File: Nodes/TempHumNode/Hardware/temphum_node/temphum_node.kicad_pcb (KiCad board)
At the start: 2 copper layers, 91.6 x 51.3 mm, 69 parts, among them IC1 CC1310F128RGZR, IC2 TPD6E004RSER, J1 TC2050-IDC, U1 MCP73123-22SI/MF, U2 SHT35-DIS-B, U3 TPS22860DBVR, U4 TPS63900DSKR, U5 MCP3421A0T-E/CH, U6 TPS22860DBVR, U7 ECS-240-9-33B-CWN-TR, X1 FC-135R

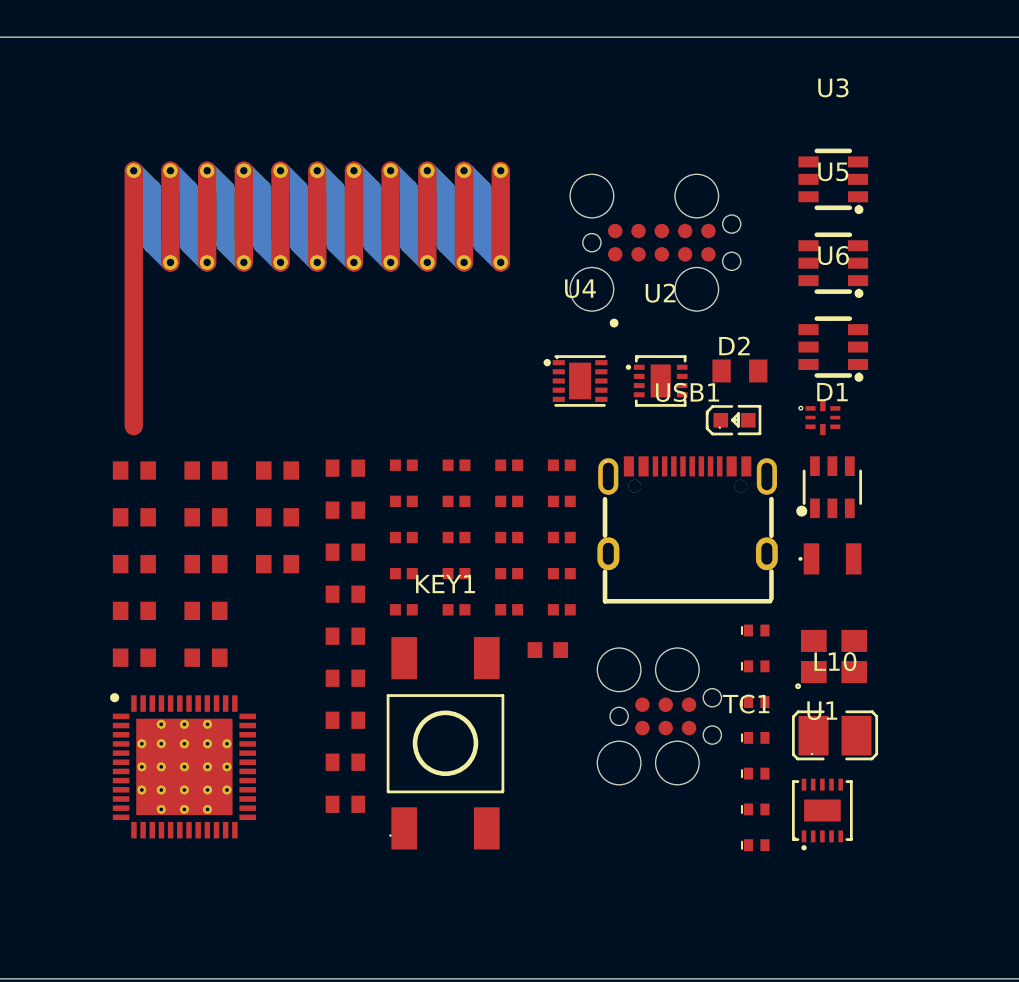
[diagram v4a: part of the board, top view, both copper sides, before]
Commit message: hw(temphum-node): add battery connector (JST B2B-PH-K-S placeholder)
Add JST PH 2.0mm 2-pin top-entry THT connector (LCSC C131337) as the
battery input placeholder. Top-entry chosen (lead internal to the
enclosure). To be confirmed against the actual pack Tue: connector
family (PH vs XH) + which pin is BAT+.

Co-Authored-By: Claude Opus 4.8 (1M context) <noreply@anthropic.com>
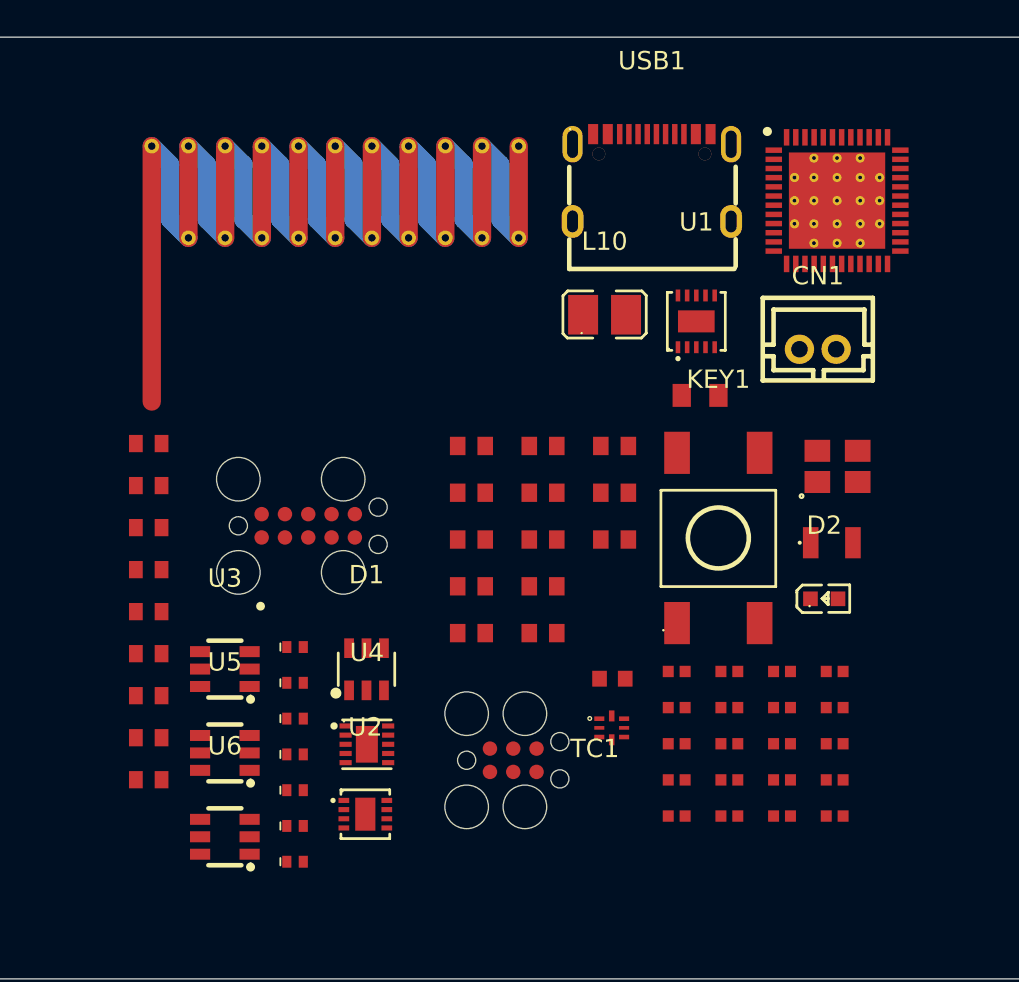
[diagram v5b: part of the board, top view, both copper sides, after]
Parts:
- added CN1: B2B-PH-K-S, SmartHome:CONN-TH_B2B-PH-K-S, F.Cu at (172.6, 33.6)
- moved IC1 47.1 mm to (173.7, 25.5)
- moved U3 42.6 mm to (140.3, 51.0)
- moved U5 42.6 mm to (140.3, 55.6)
- moved U6 42.6 mm to (140.3, 60.1)
- moved U2 28.6 mm to (148.0, 58.9)
- moved U1 27.5 mm to (166.0, 32.0)
- moved D1 27.3 mm to (148.0, 51.0)
- moved L10 26.2 mm to (161.0, 31.7)
- moved L1 25.2 mm to (144.1, 49.8)
- moved L2 25.2 mm to (144.1, 51.7)
- moved L3 25.2 mm to (144.1, 53.7)
- moved L4 25.2 mm to (144.1, 55.6)
- moved L5 25.2 mm to (144.1, 57.6)
- moved L6 25.2 mm to (144.1, 59.5)
- moved L7 25.2 mm to (144.1, 61.5)
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
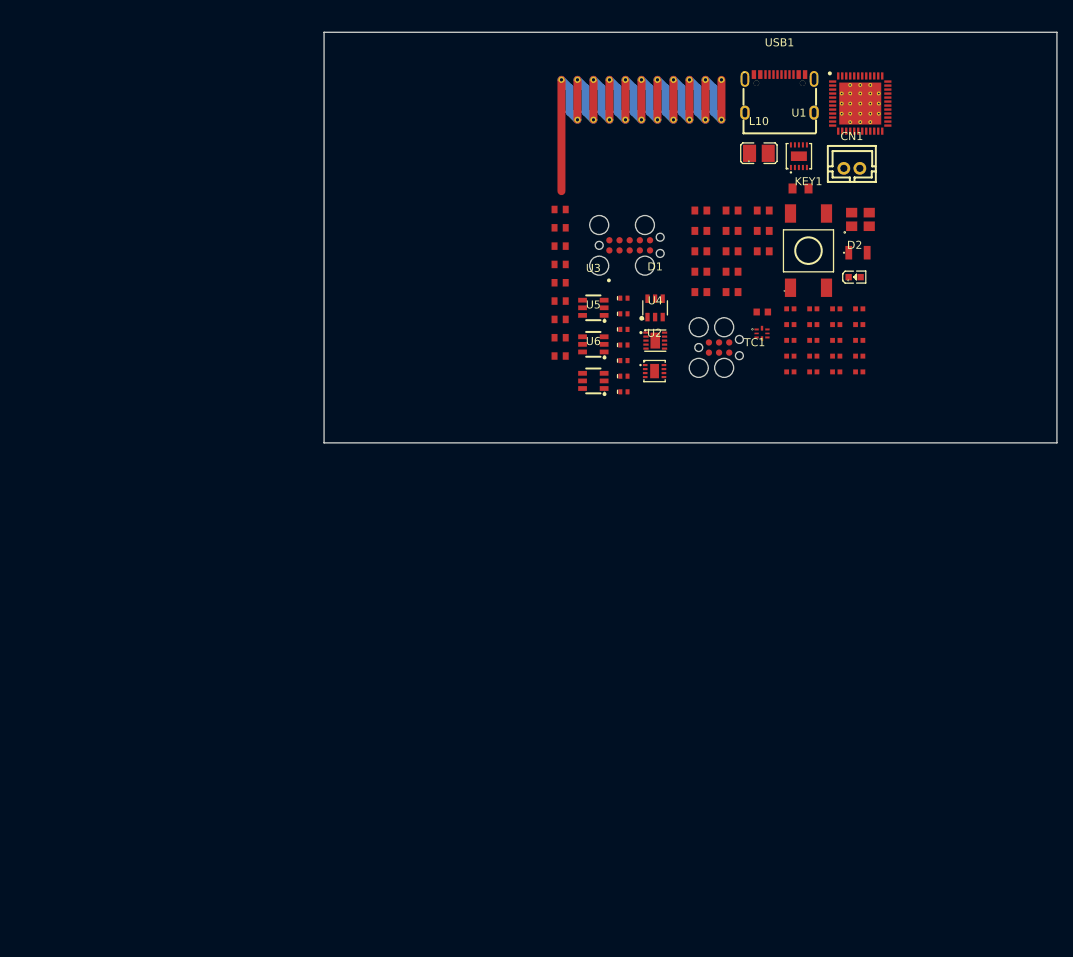
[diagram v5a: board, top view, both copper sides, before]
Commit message: hw(temphum): rev2 node schematic + PCB layout + KiCad lib parts
Full rev-2 T&H node hardware: wired schematic, 4-layer PCB layout
(RF-first placement, GND stitching, DRC-clean). Library additions:
JST XH 2.5mm connector (C158012), R_0402, and imported/perfected
footprints. USB-C center holes fixed to NPTH (annular-ring clean).

Co-Authored-By: Claude Opus 4.8 (1M context) <noreply@anthropic.com>
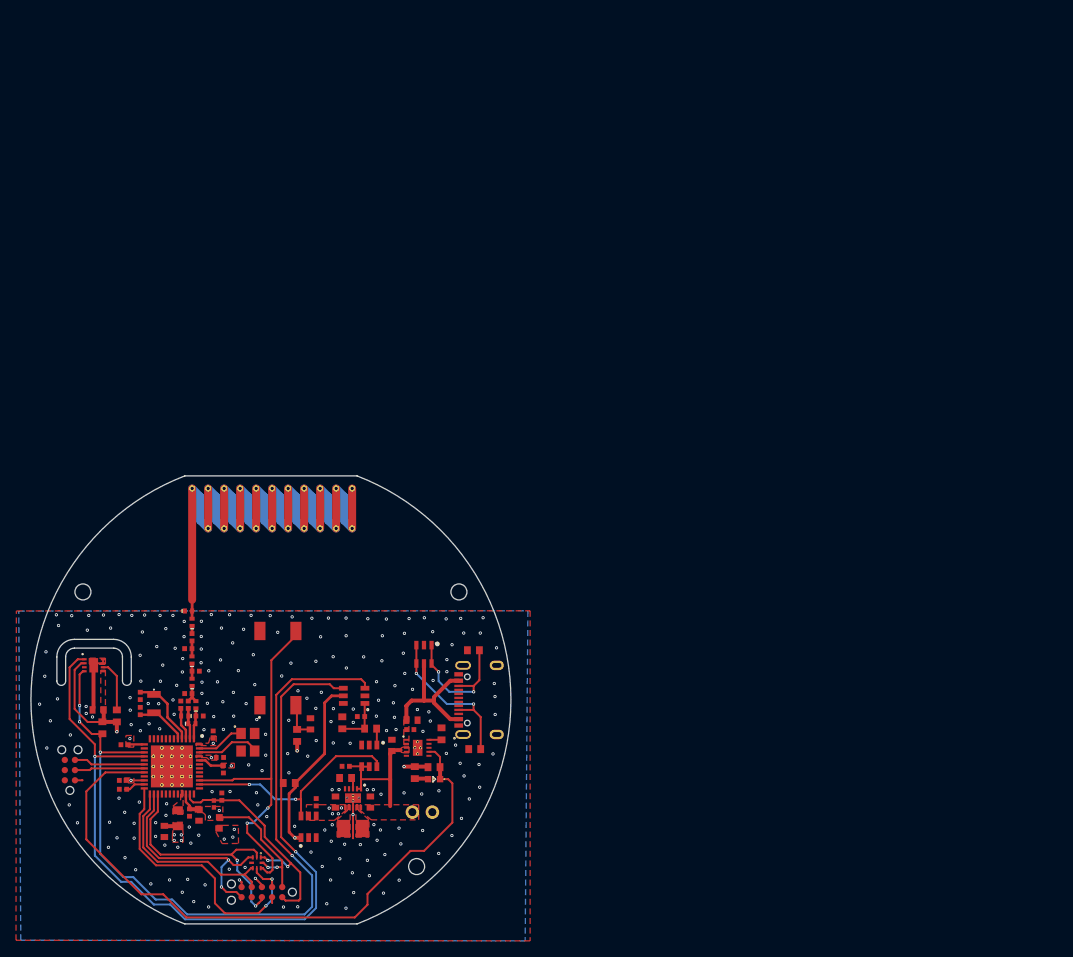
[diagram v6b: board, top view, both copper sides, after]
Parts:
- removed CN1: B2B-PH-K-S, SmartHome:CONN-TH_B2B-PH-K-S
- added CN2: B2B-XH-A, SmartHome:CONN-TH_B2B-XH-A-LF-SN, B.Cu at (118.9, 114.0)
- C25: footprint SmartHome:C_0603 -> SmartHome:C_0402
- R13: footprint SmartHome:R_0603 -> SmartHome:R_0402
- moved IC1 119.5 mm to (87.6, 108.3), turned to -90 degrees
- moved L11 110.7 mm to (88.4, 114.8), turned to -90 degrees
- moved C15 105.3 mm to (81.5, 111.2), turned to 180 degrees
- moved X1 104.5 mm to (85.4, 100.5), turned to -90 degrees
- moved C16 101.4 mm to (81.7, 105.6), turned to 180 degrees
- moved U7 100.7 mm to (97.1, 105.3), turned to -90 degrees
- moved C5 99.9 mm to (81.5, 110.1), turned to 180 degrees
- moved C14 99.5 mm to (83.7, 101.4), turned to 90 degrees
- moved L10 98.5 mm to (110.3, 116.1), turned to 180 degrees
- moved C20 97.6 mm to (93.6, 107.2)
- moved R13 97.4 mm to (92.9, 113.0), turned to 90 degrees
- moved TC1 96.8 mm to (74.9, 108.8), turned to 90 degrees
- moved C4 96.8 mm to (89.8, 114.1), turned to -90 degrees
- moved C9 96.1 mm to (83.7, 99.5), turned to -90 degrees
- moved C13 95.7 mm to (88.7, 100.6), turned to 90 degrees
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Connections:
- D1 pad 1: CC1 -> CC2
- D1 pad 3: CC2 -> CC1
- D1 pad 4: CC2 -> CC1
- D1 pad 6: CC1 -> CC2
- IC1 pad 10: PERIPH_EN -> unconnected-(IC1-DIO_5-Pad10)
- IC1 pad 11: nBUTTON -> unconnected-(IC1-DIO_6-Pad11)
- IC1 pad 12: nCHRGSTAT -> unconnected-(IC1-DIO_7-Pad12)
- IC1 pad 15: unconnected-(IC1-DIO_9-Pad15) -> SCL
- IC1 pad 16: unconnected-(IC1-DIO_10-Pad16) -> SDA
- IC1 pad 18: unconnected-(IC1-DIO_12-Pad18) -> UART_TX
- IC1 pad 19: unconnected-(IC1-DIO_13-Pad19) -> UART_RX
- IC1 pad 20: unconnected-(IC1-DIO_14-Pad20) -> nCHRGSTAT
- IC1 pad 21: JTAG_TDO -> unconnected-(IC1-DIO_15-Pad21)
- IC1 pad 26: JTAG_TDI -> JTAG_TDO
- IC1 pad 27: unconnected-(IC1-DIO_17-Pad27) -> JTAG_TDI
- IC1 pad 38: unconnected-(IC1-DIO_25-Pad38) -> PERIPH_EN
- IC1 pad 39: unconnected-(IC1-DIO_26-Pad39) -> nBUTTON
- IC1 pad 6: SCL -> unconnected-(IC1-DIO_1-Pad6)
- IC1 pad 7: SDA -> unconnected-(IC1-DIO_2-Pad7)
- IC1 pad 8: UART_TX -> unconnected-(IC1-DIO_3-Pad8)
- IC1 pad 9: UART_RX -> unconnected-(IC1-DIO_4-Pad9)
- TC1 pad 2: UART_TX -> unconnected-(TC1-~-Pad2)
- TC1 pad 5: unconnected-(TC1-~-Pad5) -> UART_TX
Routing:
- net SCL: track 0.00 -> 102.1 mm, vias 0 -> 4
- net SDA: track 0.00 -> 101.6 mm, vias 0 -> 2
- net nCHRGSTAT: track 0.00 -> 80.8 mm
- net 3V3_SW: track 0.00 -> 76.9 mm, vias 0 -> 2
- net VDDS: track 0.00 -> 63.7 mm, vias 0 -> 7
- net nBUTTON: track 0.00 -> 45.0 mm, vias 0 -> 2
- net JTAG_TMS: track 0.00 -> 36.6 mm, vias 0 -> 2
- net 3V3: track 0.00 -> 36.0 mm, vias 0 -> 9
- net JTAG_TDI: track 0.00 -> 30.6 mm, vias 0 -> 2
- net nRESET: track 0.00 -> 29.6 mm, vias 0 -> 2
- net PERIPH_EN: track 0.00 -> 28.8 mm, vias 0 -> 2
- net JTAG_TDO: track 0.00 -> 28.3 mm, vias 0 -> 2
- net JTAG_TCK: track 0.00 -> 24.4 mm
- net CC1: track 0.00 -> 20.2 mm, vias 0 -> 2
- net VBUS: track 0.00 -> 18.7 mm
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- added copper zone on F.Cu, net 3V3
- added copper zone on In2.Cu, net 3V3
- added copper zone on F.Cu, net 3V3_SW
- added copper zone on F.Cu, net BAT+
- added copper zone on F.Cu, net DCDC_SW
- added copper zone on B.Cu, net GND
- added copper zone on F.Cu, net GND
- added copper zone on In1.Cu, net GND
- added copper zone on In2.Cu, net GND
- added copper zone on F.Cu, net Net-(U4-LX1)
- added copper zone on F.Cu, net Net-(U4-LX2)
- added copper zone on F.Cu, net VBUS
- added copper zone on F.Cu, net VDDR
- added copper zone on In2.Cu, net VDDR
- added copper zone on F.Cu, net VDDS
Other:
- board size 91.6 x 51.3 mm -> 60 x 56 mm
- copper layers 2 -> 4
- board text added: "+"
- board text added: "-"
- board text added: "LiFePO4"

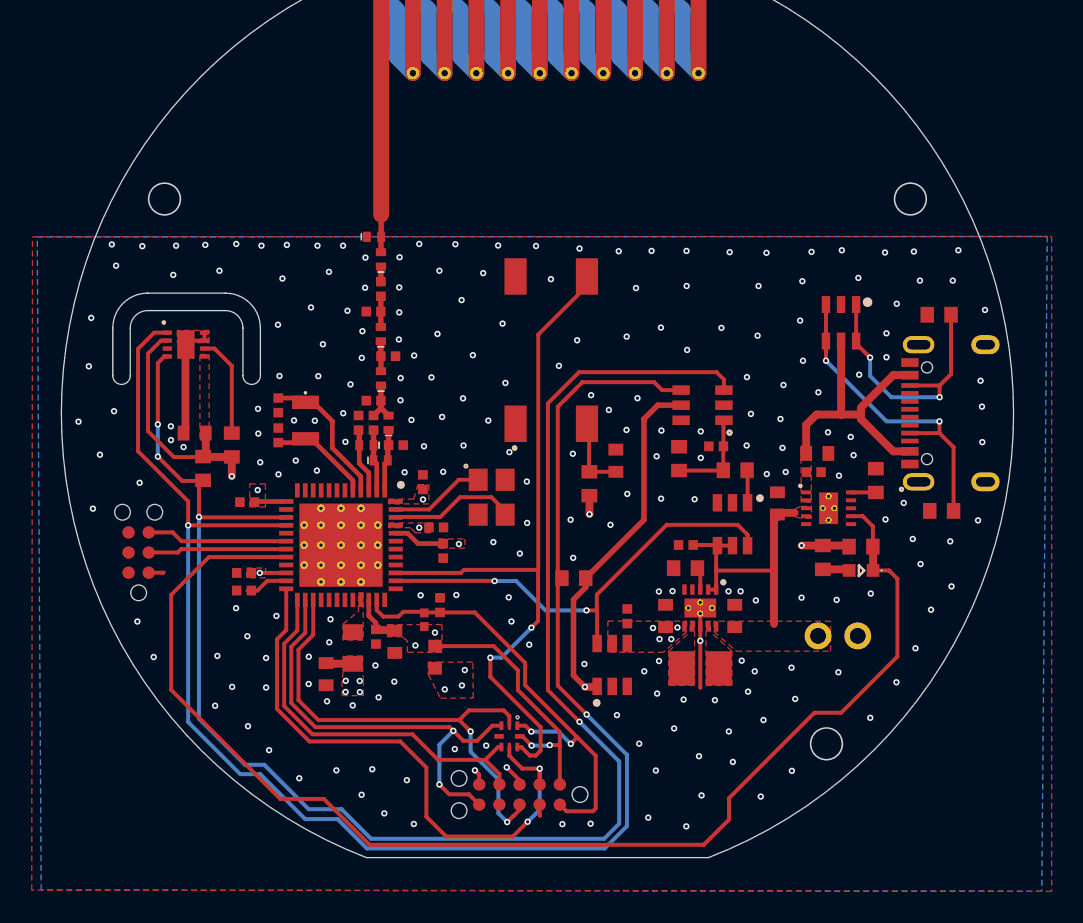
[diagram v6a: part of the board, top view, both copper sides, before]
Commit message: hw(temphum): rev2 production-ready — sent to JLCPCB
Footprints refined to TI/Microchip datasheets: CC1310 EP paste windowpane
(dodges thermal vias) + 0.24mm roundrect pads + NSMD 0.05; DFN charger &
WSON regulator EP paste segmentation; USB-C center holes NPTH + 0.65 drill.
XH battery connector, AITRONIC logo, GND stitching, silkscreen. Full LCSC
BOM + CPL + Gerbers (3 assembled protos ordered).

Co-Authored-By: Claude Opus 4.8 (1M context) <noreply@anthropic.com>
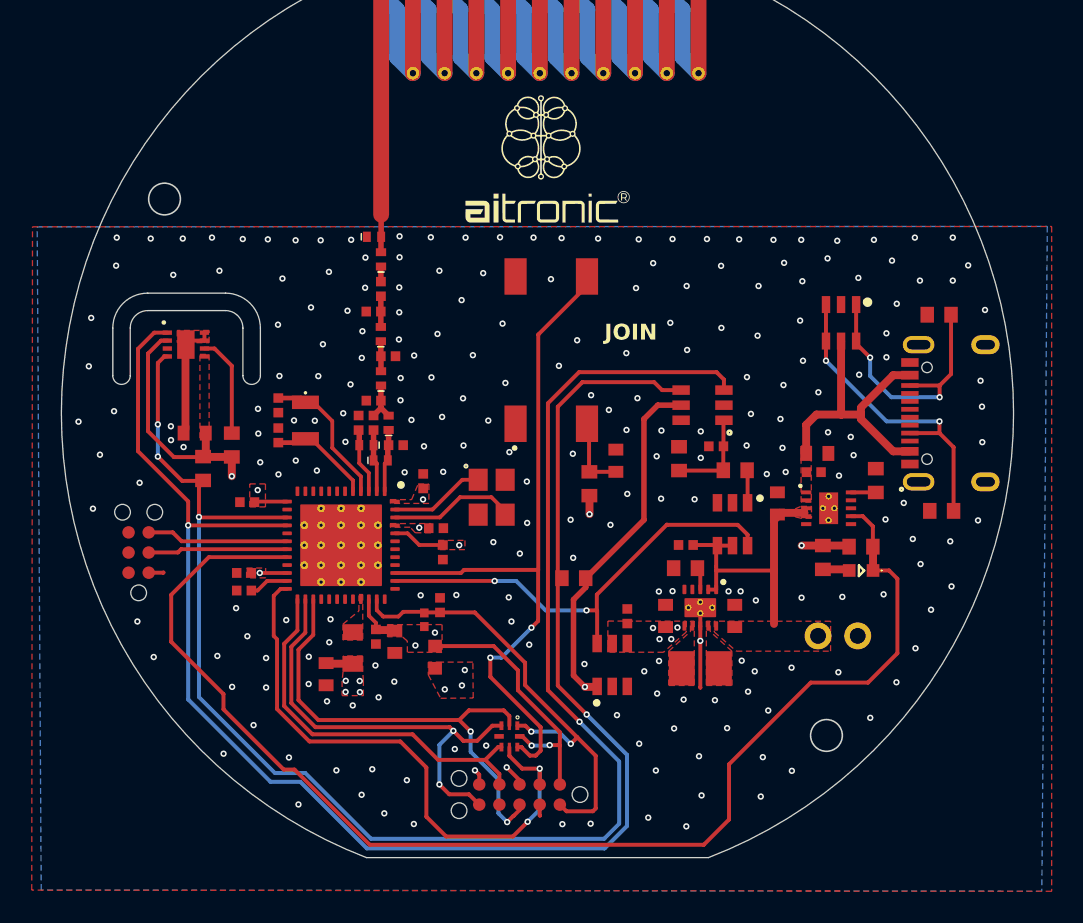
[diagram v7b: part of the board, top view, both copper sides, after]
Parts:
- added G***: LOGO, SmartHome:LOGO_AITRONIC, F.Cu at (100.5, 84.0)
- moved C18 0.09 mm to (94.0, 108.8)
- moved C21 0.06 mm to (92.8, 104.3)
- moved C20 0.05 mm to (93.6, 107.2)
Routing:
- net BAT+: track 17.2 -> 18.4 mm
- net SDA: track 101.6 -> 100.9 mm
- net SCL: track 102.1 -> 101.3 mm
- net GND: vias 225 -> 232
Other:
- outline, holes or cut-outs redrawn
- board text added: "JOIN"
- board text added: "TEMPHUM-NODE REV2 2026-07"
